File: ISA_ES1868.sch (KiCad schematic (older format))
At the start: 105 parts, among them J1 LINE IN, J10 Vol. Btns, J11 ISA BUS, J2 LINE OUT, J3 Joystick/MIDI, J5 Wavetable, J7 SPKR OUT, J8 MIC IN, U1 L78L05, U2 74LS138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

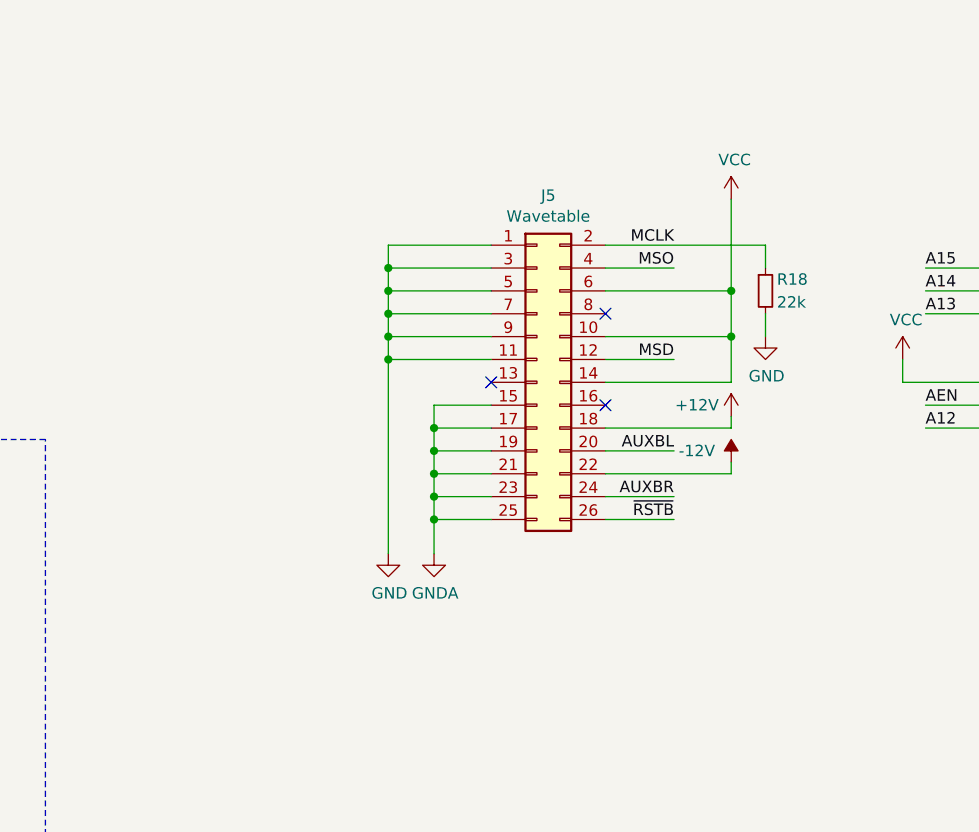
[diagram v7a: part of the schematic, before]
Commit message: Add selection to invert channels from wavetable
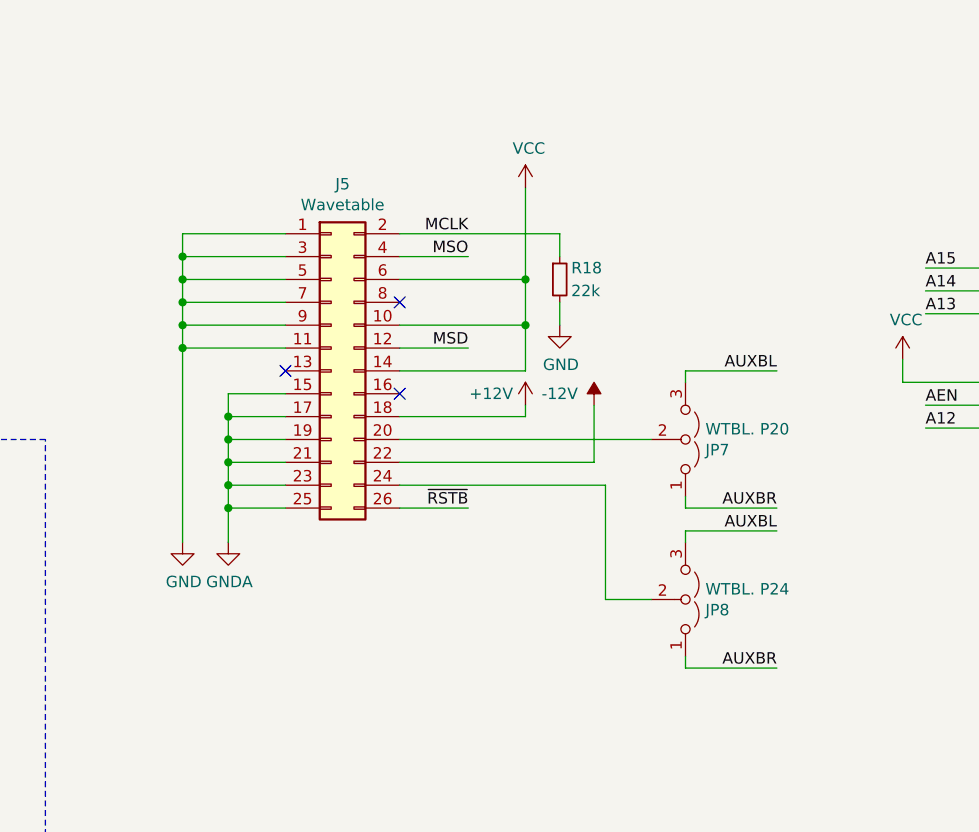
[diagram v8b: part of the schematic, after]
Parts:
- added JP7: WTBL. P20, Jumper:SolderJumper-3_P1.3mm_Open_RoundedPad1.0x1.5mm_NumberLabels, symbol Jumper:Jumper_3_Open
- added JP8: WTBL. P24, Jumper:SolderJumper-3_P1.3mm_Open_RoundedPad1.0x1.5mm_NumberLabels, symbol Jumper:Jumper_3_Open
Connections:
- net AUXBL: now also JP7.3 (B), JP8.3 (B); no longer J5.20 (Pin_20)
- net AUXBR: now also JP7.1 (A), JP8.1 (A); no longer J5.24 (Pin_24)
- new net: J5.20 (Pin_20), JP7.2 (C)
- new net: J5.24 (Pin_24), JP8.2 (C)
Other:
- moved on the sheet: J5, R18
